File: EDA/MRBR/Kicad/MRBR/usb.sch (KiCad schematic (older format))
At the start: 14 parts, among them J1 TYPE-C-31-M-12, Q1 MMBT489LT1G, Q2 MMBT489LT1G, U3 FT232RL

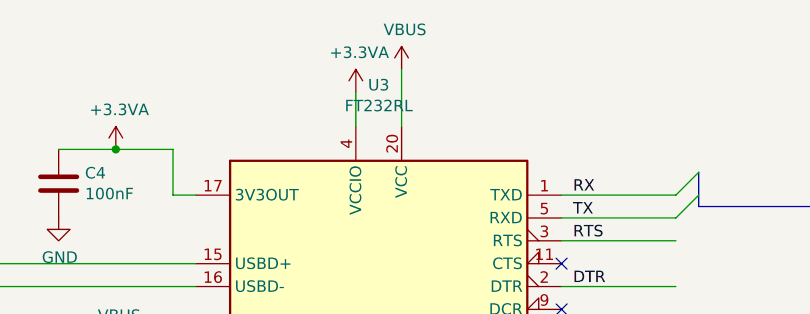
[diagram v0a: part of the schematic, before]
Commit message: Added barrel jack to PSU
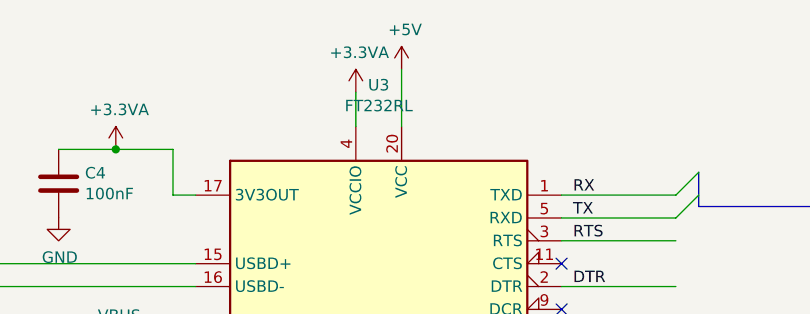
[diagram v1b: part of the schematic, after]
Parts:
- J1: footprint HRO_TYPE-C-31-M-12 -> Connector_USB:HRO_TYPE-C-31-M-12
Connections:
- net labels added: +5V
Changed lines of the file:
@@
 Wire Wire Line
 	4950 1550 5200 1550
-$Comp
-L power:VBUS #PWR020
-U 1 1 611E44BF
-P 6450 1200
-F 0 "#PWR020" H 6450 1050 50  0001 C CNN
-F 1 "VBUS" H 6465 1373 50  0000 C CNN
-F 2 "" H 6450 1200 50  0001 C CNN
-F 3 "" H 6450 1200 50  0001 C CNN
-	1    6450 1200
-	1    0    0    -1
-$EndComp
 Wire Wire Line
 	6450 1200 6450 1450
@@
 F 0 "J1" H 2450 2817 50  0000 C CNN
 F 1 "TYPE-C-31-M-12" H 2450 2726 50  0000 C CNN
-F 2 "HRO_TYPE-C-31-M-12" H 2450 2150 50  0001 L BNN
+F 2 "Connector_USB:HRO_TYPE-C-31-M-12" H 2450 2150 50  0001 L BNN
 F 3 "" H 2450 2150 50  0001 L BNN
 F 4 "3.31mm" H 2450 2150 50  0001 L BNN "MAXIMUM_PACKAGE_HEIGHT"
@@
 Wire Wire Line
 	1750 2450 1750 2550
-Wire Bus Line
-	7750 1650 7750 1800
 $Comp
 L power:GND #PWR011
@@
 $EndComp
 Connection ~ 1750 2550
+Wire Bus Line
+	7750 1650 7750 1800
+$Comp
+L power:+5V #PWR06
+U 1 1 6126FC6E
+P 6450 1200
+F 0 "#PWR06" H 6450 1050 50  0001 C CNN
+F 1 "+5V" H 6465 1373 50  0000 C CNN
+F 2 "" H 6450 1200 50  0001 C CNN
+F 3 "" H 6450 1200 50  0001 C CNN
+	1    6450 1200
+	1    0    0    -1
+$EndComp
 $EndSCHEMATC
